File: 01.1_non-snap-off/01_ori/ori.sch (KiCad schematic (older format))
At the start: 141 parts, among them J1 TYPE-C-31-M12_13, J2 AVR-ISP-6_mod, K1 KEYSW, K10 KEYSW, K11 KEYSW, K12 KEYSW, K13 KEYSW, K14 KEYSW, K15 KEYSW, K16 KEYSW, K17 KEYSW, K18 KEYSW, K19 KEYSW, K2 KEYSW, K20 KEYSW, K21 KEYSW, K22 KEYSW, K23 KEYSW, K24 KEYSW, K25 KEYSW, K26 KEYSW, K27 KEYSW, K28 KEYSW, K29 KEYSW, K3 KEYSW, K30 KEYSW, K31 KEYSW, K32 KEYSW, K33 KEYSW, K34 KEYSW, K35 KEYSW, K36 KEYSW, K37 KEYSW, K38 KEYSW, K39 KEYSW, K4 KEYSW, K40 KEYSW, K41 KEYSW, K42 KEYSW, K43 KEYSW, K44 KEYSW, K45 KEYSW, K46 KEYSW, K47 KEYSW, K48 KEYSW, K49 KEYSW, K5 KEYSW, K50 KEYSW, K51 KEYSW, K52 KEYSW, K6 KEYSW, K7 KEYSW, K8 KEYSW, K9 KEYSW, SW1 SW_PUSH, SW2 Rotary_Encoder_Switch, U1 ATMEGA32U4, U3 USBLC6-2SC6, Y1 16MHz

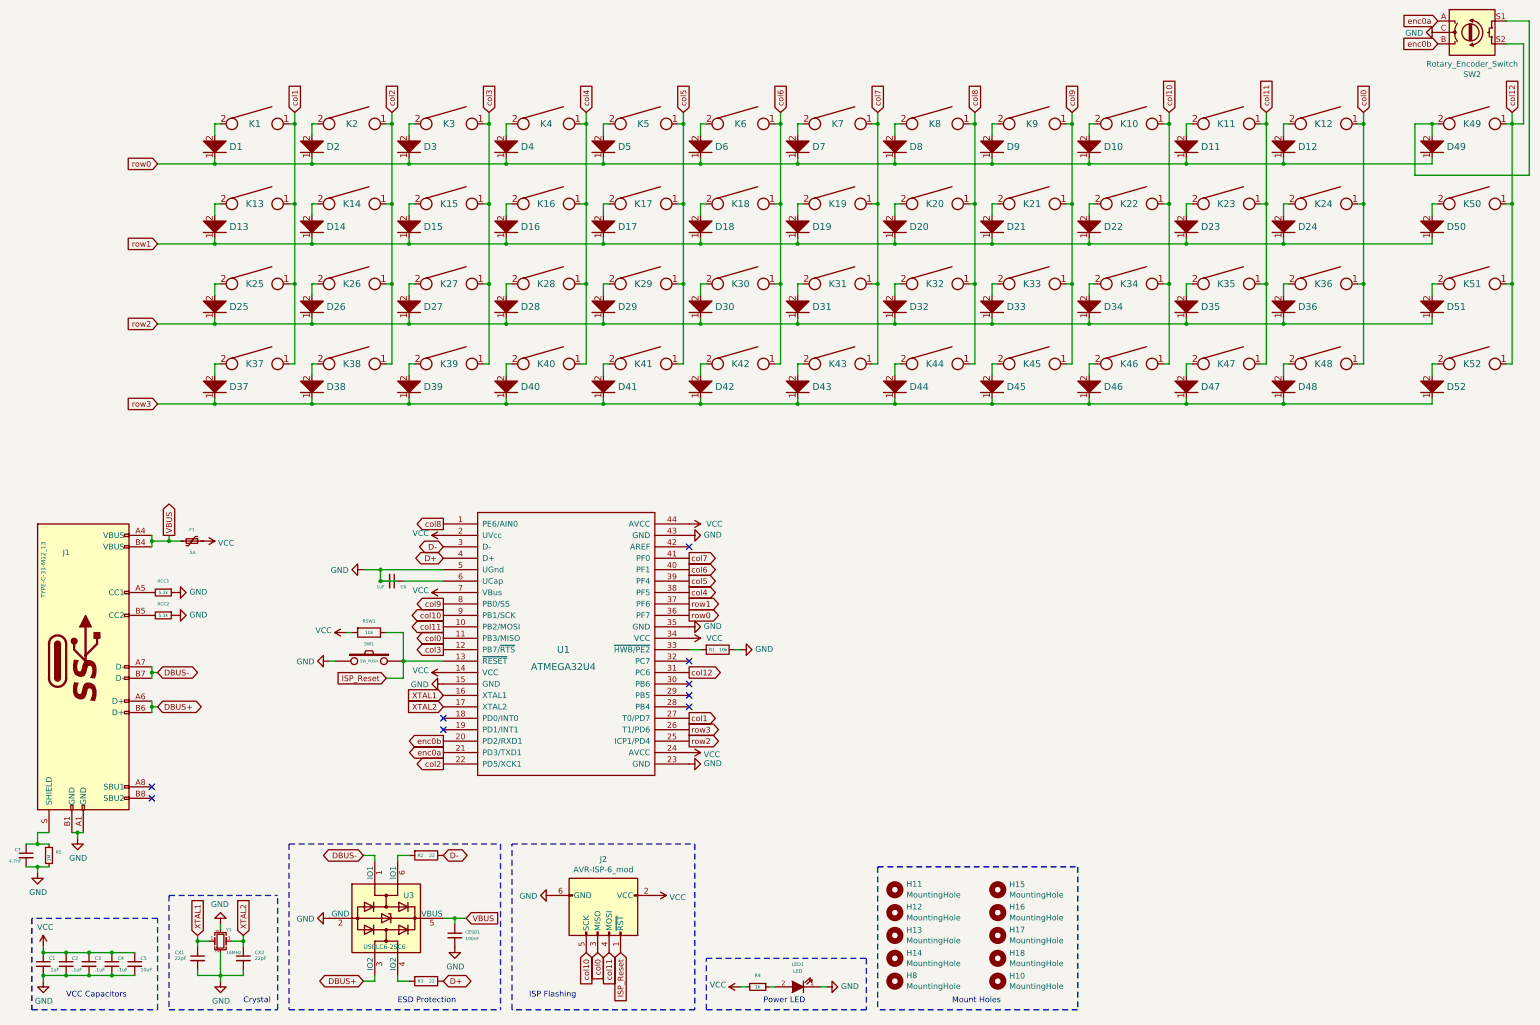
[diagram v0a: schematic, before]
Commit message: update column names
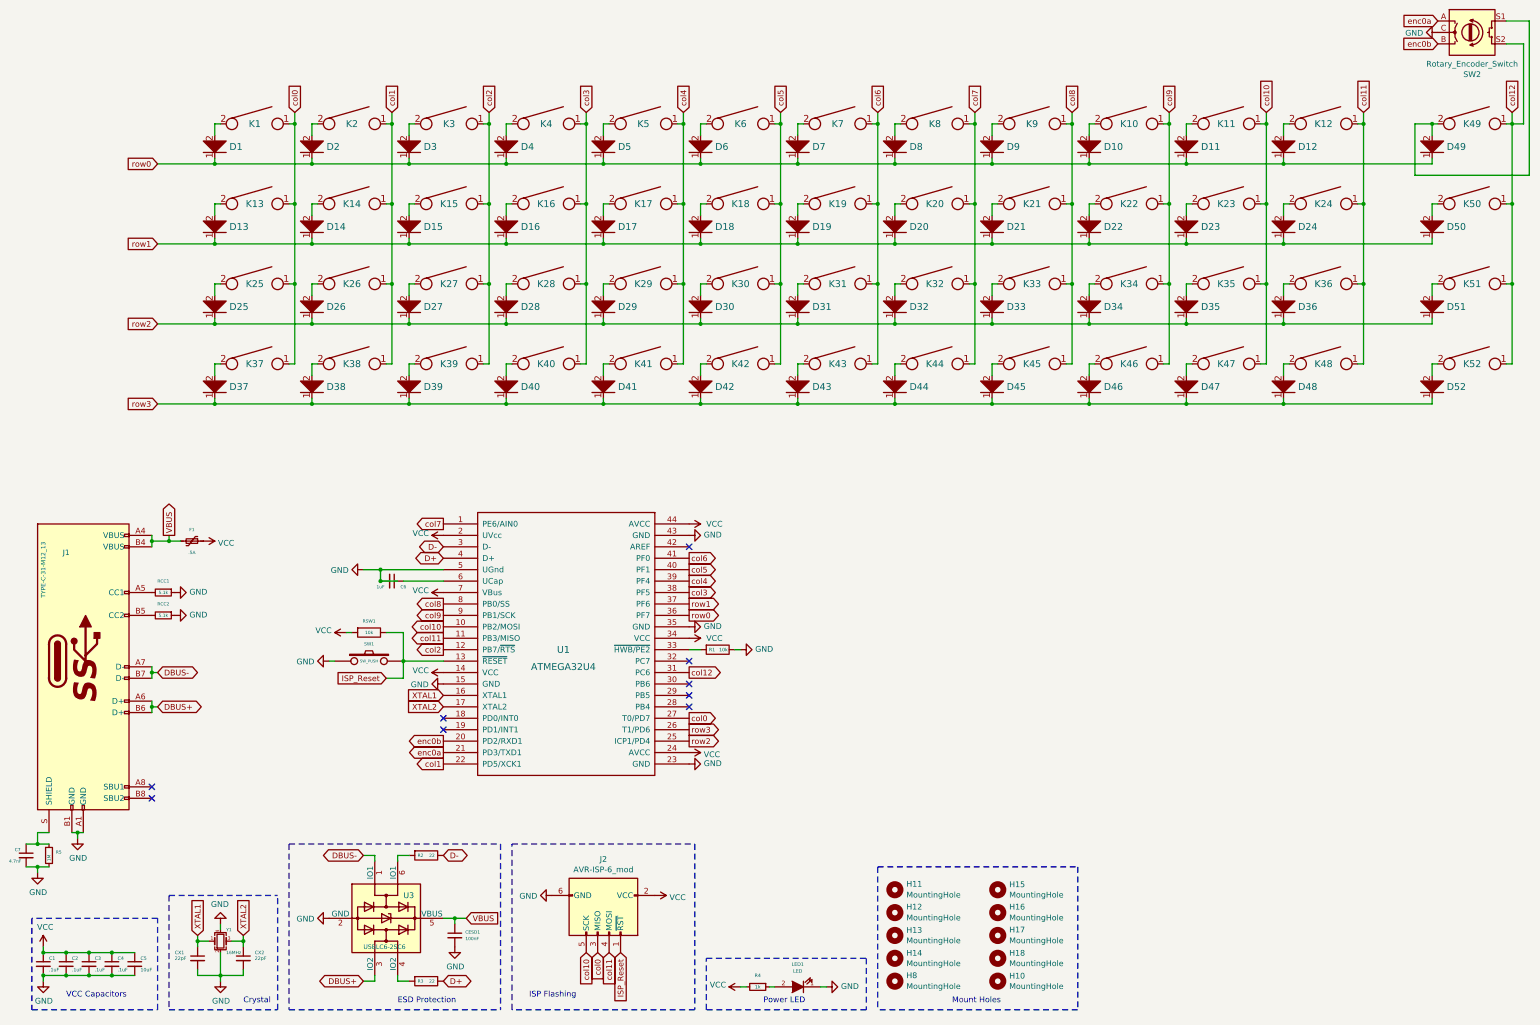
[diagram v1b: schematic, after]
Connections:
- net col0: now also K1.1, K13.1, K25.1, K37.1, U1.27 (T0/PD7); no longer K12.1, K24.1, K36.1, K48.1, U1.11 (PB3/MISO)
- net col1: now also K14.1, K2.1, K26.1, K38.1, U1.22 (PD5/XCK1); no longer K1.1, K13.1, K25.1, K37.1, U1.27 (T0/PD7)
- net col10: now also K11.1, K23.1, K35.1, K47.1, U1.10 (PB2/MOSI); no longer K10.1, K22.1, K34.1, K46.1, U1.9 (PB1/SCK)
- net col11: now also K12.1, K24.1, K36.1, K48.1, U1.11 (PB3/MISO); no longer K11.1, K23.1, K35.1, K47.1, U1.10 (PB2/MOSI)
- net col2: now also K15.1, K27.1, K3.1, K39.1, U1.12 (PB7/~RTS); no longer K14.1, K2.1, K26.1, K38.1, U1.22 (PD5/XCK1)
- net col3: now also K16.1, K28.1, K4.1, K40.1, U1.38 (PF5); no longer K15.1, K27.1, K3.1, K39.1, U1.12 (PB7/~RTS)
- net col4: now also K17.1, K29.1, K41.1, K5.1, U1.39 (PF4); no longer K16.1, K28.1, K4.1, K40.1, U1.38 (PF5)
- net col5: now also K18.1, K30.1, K42.1, K6.1, U1.40 (PF1); no longer K17.1, K29.1, K41.1, K5.1, U1.39 (PF4)
- net col6: now also K19.1, K31.1, K43.1, K7.1, U1.41 (PF0); no longer K18.1, K30.1, K42.1, K6.1, U1.40 (PF1)
- net col7: now also K20.1, K32.1, K44.1, K8.1, U1.1 (PE6/AIN0); no longer K19.1, K31.1, K43.1, K7.1, U1.41 (PF0)
- net col8: now also K21.1, K33.1, K45.1, K9.1, U1.8 (PB0/SS); no longer K20.1, K32.1, K44.1, K8.1, U1.1 (PE6/AIN0)
- net col9: now also K10.1, K22.1, K34.1, K46.1, U1.9 (PB1/SCK); no longer K21.1, K33.1, K45.1, K9.1, U1.8 (PB0/SS)
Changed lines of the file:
@@
 row1
 Text GLabel 5300 7400 0    50   Output ~ 0
+col1
+Text GLabel 5300 6400 0    50   Output ~ 0
 col2
-Text GLabel 5300 6400 0    50   Output ~ 0
-col3
 Text GLabel 5300 6200 0    50   Output ~ 0
-col11
+col10
 Text GLabel 5300 6100 0    50   Output ~ 0
-col10
+col9
 Text GLabel 5300 6000 0    50   Output ~ 0
-col9
+col8
 Text GLabel 5300 5300 0    50   Output ~ 0
-col8
+col7
 Text GLabel 7450 6100 2    50   Output ~ 0
 row0
@@
 $EndComp
 Text GLabel 7450 5800 2    50   Output ~ 0
+col4
+Text GLabel 7450 5700 2    50   Output ~ 0
 col5
-Text GLabel 7450 5700 2    50   Output ~ 0
-col6
-Text GLabel 7450 5600 2    50   Output ~ 0
-col7
 NoConn ~ 7450 5500
 Text GLabel 5300 9300 2    50   BiDi ~ 0
@@
 $EndComp
 Text GLabel 7450 5900 2    50   Output ~ 0
-col4
+col3
 Text GLabel 7450 7100 2    50   Output ~ 0
 row3
@@
 $EndComp
 Connection ~ 14650 2500
-Text GLabel 13350 1700 1    50   Input ~ 0
-col0
-Text GLabel 5300 6300 0    50   Output ~ 0
+Text GLabel 4000 1700 1    50   Input ~ 0
 col0
 Wire Wire Line
@@
 	13350 2500 13350 3200
 Connection ~ 13350 2500
-Text GLabel 4000 1700 1    50   Input ~ 0
+Text GLabel 4850 1700 1    50   Input ~ 0
 col1
-Text GLabel 4850 1700 1    50   Input ~ 0
+Text GLabel 5700 1700 1    50   Input ~ 0
 col2
-Text GLabel 5700 1700 1    50   Input ~ 0
+Text GLabel 6550 1700 1    50   Input ~ 0
 col3
-Text GLabel 6550 1700 1    50   Input ~ 0
+Text GLabel 7400 1700 1    50   Input ~ 0
 col4
-Text GLabel 7400 1700 1    50   Input ~ 0
+Text GLabel 8250 1700 1    50   Input ~ 0
 col5
-Text GLabel 8250 1700 1    50   Input ~ 0
+Text GLabel 9100 1700 1    50   Input ~ 0
 col6
-Text GLabel 9100 1700 1    50   Input ~ 0
+Text GLabel 9950 1700 1    50   Input ~ 0
 col7
-Text GLabel 9950 1700 1    50   Input ~ 0
+Text GLabel 10800 1700 1    50   Input ~ 0
 col8
-Text GLabel 10800 1700 1    50   Input ~ 0
+Text GLabel 11650 1700 1    50   Input ~ 0
 col9
-Text GLabel 11650 1700 1    50   Input ~ 0
-col10
-Text GLabel 12500 1700 1    50   Input ~ 0
+Text GLabel 13350 1700 1    50   Input ~ 0
 col11
 Text GLabel 14650 1700 1    50   Input ~ 0
@@
 enc0a
 Text GLabel 7450 7000 2    50   Output ~ 0
-col1
+col0
 Text GLabel 2800 4250 0    50   Input ~ 0
 row3
@@
 Wire Notes Line
 	9100 8300 9100 9550
+Text GLabel 12500 1700 1    50   Input ~ 0
+col10
+Text GLabel 5300 6300 0    50   Output ~ 0
+col11
+Text GLabel 7450 5600 2    50   Output ~ 0
+col6
 $EndSCHEMATC

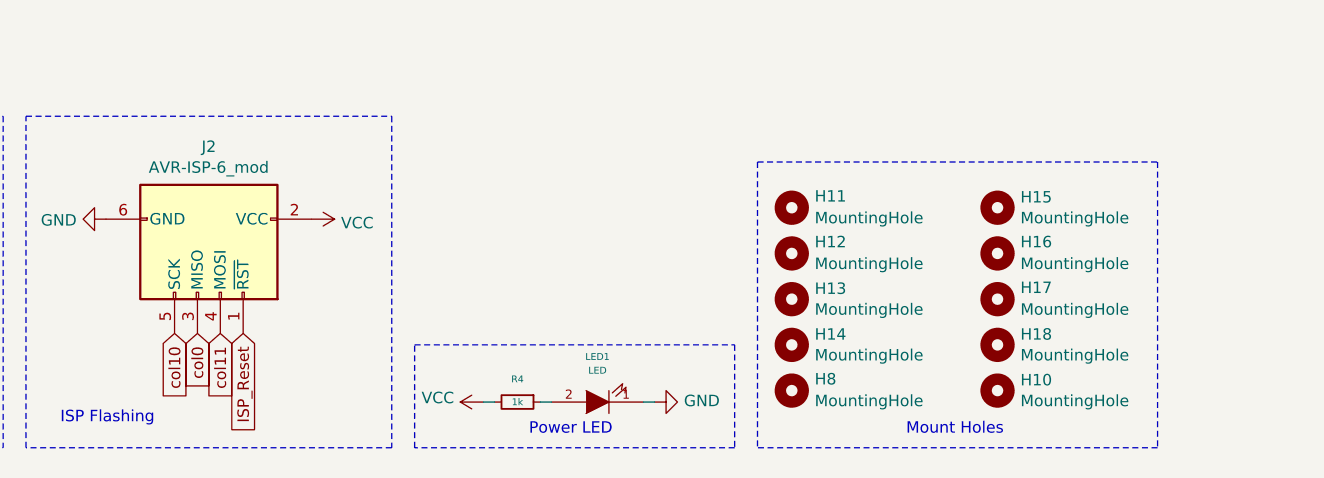
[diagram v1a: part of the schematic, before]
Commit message: moved mounting holes
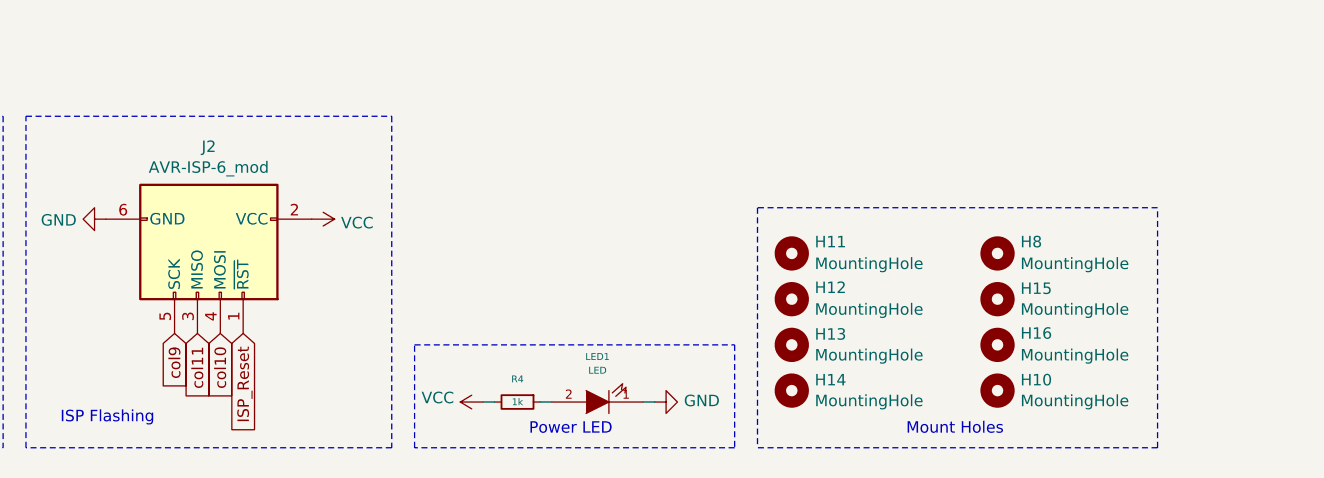
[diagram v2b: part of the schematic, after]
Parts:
- removed H17, H18: MountingHole, random-keyboard-parts:plate_hole_4mm_tht, symbol Mechanical:MountingHole
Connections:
- net col0: no longer J2.3 (MISO)
- net col10: now also J2.4 (MOSI); no longer J2.5 (SCK)
- net col11: now also J2.3 (MISO); no longer J2.4 (MOSI)
- net col9: now also J2.5 (SCK)
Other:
- moved on the sheet: H11, H12, H13, H14, H15, H16, H8
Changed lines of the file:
@@
 L Mechanical:MountingHole H8
 U 1 1 5F26174E
-P 9250 9300
-F 0 "H8" H 9350 9350 50  0000 L CNN
-F 1 "MountingHole" H 9350 9255 50  0000 L CNN
-F 2 "random-keyboard-parts:plate_hole_4mm_tht" H 9250 9300 50  0001 C CNN
-F 3 "~" H 9250 9300 50  0001 C CNN
-	1    9250 9300
+P 10150 8700
+F 0 "H8" H 10250 8750 50  0000 L CNN
+F 1 "MountingHole" H 10250 8655 50  0000 L CNN
+F 2 "random-keyboard-parts:plate_hole_4mm_tht" H 10150 8700 50  0001 C CNN
+F 3 "~" H 10150 8700 50  0001 C CNN
+	1    10150 8700
 	1    0    0    -1
 $EndComp
@@
 	1    0    0    -1
 $EndComp
-Wire Notes Line
-	9100 8300 10850 8300
 Text Notes 9750 9500 0    50   ~ 0
 Mount Holes
 $Comp
-L Mechanical:MountingHole H17
-U 1 1 5EC1BF9B
+L Mechanical:MountingHole H15
+U 1 1 5EC1BF95
 P 10150 8900
-F 0 "H17" H 10250 8950 50  0000 L CNN
+F 0 "H15" H 10250 8946 50  0000 L CNN
 F 1 "MountingHole" H 10250 8855 50  0000 L CNN
 F 2 "random-keyboard-parts:plate_hole_4mm_tht" H 10150 8900 50  0001 C CNN
@@
 $EndComp
 $Comp
-L Mechanical:MountingHole H15
-U 1 1 5EC1BF95
-P 10150 8500
-F 0 "H15" H 10250 8546 50  0000 L CNN
-F 1 "MountingHole" H 10250 8455 50  0000 L CNN
-F 2 "random-keyboard-parts:plate_hole_4mm_tht" H 10150 8500 50  0001 C CNN
-F 3 "~" H 10150 8500 50  0001 C CNN
-	1    10150 8500
-	1    0    0    -1
-$EndComp
-$Comp
-L Mechanical:MountingHole H18
-U 1 1 5EC1BF8F
+L Mechanical:MountingHole H16
+U 1 1 5EC1BF89
 P 10150 9100
-F 0 "H18" H 10250 9146 50  0000 L CNN
+F 0 "H16" H 10250 9150 50  0000 L CNN
 F 1 "MountingHole" H 10250 9055 50  0000 L CNN
 F 2 "random-keyboard-parts:plate_hole_4mm_tht" H 10150 9100 50  0001 C CNN
@@
 $EndComp
 $Comp
-L Mechanical:MountingHole H16
-U 1 1 5EC1BF89
-P 10150 8700
-F 0 "H16" H 10250 8750 50  0000 L CNN
-F 1 "MountingHole" H 10250 8655 50  0000 L CNN
-F 2 "random-keyboard-parts:plate_hole_4mm_tht" H 10150 8700 50  0001 C CNN
-F 3 "~" H 10150 8700 50  0001 C CNN
-	1    10150 8700
-	1    0    0    -1
-$EndComp
-$Comp
 L Mechanical:MountingHole H12
 U 1 1 5EC1BF83
+P 9250 8900
+F 0 "H12" H 9350 8950 50  0000 L CNN
+F 1 "MountingHole" H 9350 8855 50  0000 L CNN
+F 2 "random-keyboard-parts:plate_hole_4mm_tht" H 9250 8900 50  0001 C CNN
+F 3 "~" H 9250 8900 50  0001 C CNN
+	1    9250 8900
+	1    0    0    -1
+$EndComp
+$Comp
+L Mechanical:MountingHole H14
+U 1 1 5EC1BF7D
+P 9250 9300
+F 0 "H14" H 9350 9346 50  0000 L CNN
+F 1 "MountingHole" H 9350 9255 50  0000 L CNN
+F 2 "random-keyboard-parts:plate_hole_4mm_tht" H 9250 9300 50  0001 C CNN
+F 3 "~" H 9250 9300 50  0001 C CNN
+	1    9250 9300
+	1    0    0    -1
+$EndComp
+$Comp
+L Mechanical:MountingHole H13
+U 1 1 5EC1BF77
+P 9250 9100
+F 0 "H13" H 9350 9146 50  0000 L CNN
+F 1 "MountingHole" H 9350 9055 50  0000 L CNN
+F 2 "random-keyboard-parts:plate_hole_4mm_tht" H 9250 9100 50  0001 C CNN
+F 3 "~" H 9250 9100 50  0001 C CNN
+	1    9250 9100
+	1    0    0    -1
+$EndComp
+$Comp
+L Mechanical:MountingHole H11
+U 1 1 5EC1BF71
 P 9250 8700
-F 0 "H12" H 9350 8750 50  0000 L CNN
+F 0 "H11" H 9350 8750 50  0000 L CNN
 F 1 "MountingHole" H 9350 8655 50  0000 L CNN
 F 2 "random-keyboard-parts:plate_hole_4mm_tht" H 9250 8700 50  0001 C CNN
 F 3 "~" H 9250 8700 50  0001 C CNN
 	1    9250 8700
-	1    0    0    -1
-$EndComp
-$Comp
-L Mechanical:MountingHole H14
-U 1 1 5EC1BF7D
-P 9250 9100
-F 0 "H14" H 9350 9146 50  0000 L CNN
-F 1 "MountingHole" H 9350 9055 50  0000 L CNN
-F 2 "random-keyboard-parts:plate_hole_4mm_tht" H 9250 9100 50  0001 C CNN
-F 3 "~" H 9250 9100 50  0001 C CNN
-	1    9250 9100
-	1    0    0    -1
-$EndComp
-$Comp
-L Mechanical:MountingHole H13
-U 1 1 5EC1BF77
-P 9250 8900
-F 0 "H13" H 9350 8946 50  0000 L CNN
-F 1 "MountingHole" H 9350 8855 50  0000 L CNN
-F 2 "random-keyboard-parts:plate_hole_4mm_tht" H 9250 8900 50  0001 C CNN
-F 3 "~" H 9250 8900 50  0001 C CNN
-	1    9250 8900
-	1    0    0    -1
-$EndComp
-$Comp
-L Mechanical:MountingHole H11
-U 1 1 5EC1BF71
-P 9250 8500
-F 0 "H11" H 9350 8550 50  0000 L CNN
-F 1 "MountingHole" H 9350 8455 50  0000 L CNN
-F 2 "random-keyboard-parts:plate_hole_4mm_tht" H 9250 8500 50  0001 C CNN
-F 3 "~" H 9250 8500 50  0001 C CNN
-	1    9250 8500
 	1    0    0    -1
 $EndComp
@@
 $EndComp
 Text GLabel 6650 9050 3    50   Input ~ 0
-col0
+col11
 Text GLabel 6750 9050 3    50   Input ~ 0
-col11
+col10
 $Comp
 L power:GND #PWR0101
@@
 D-
 Text GLabel 6550 9050 3    50   Input ~ 0
-col10
+col9
 Text GLabel 6850 9050 3    50   Input ~ 0
 ISP_Reset
@@
 Wire Notes Line
 	10850 9550 9100 9550
-Wire Notes Line
-	10850 8300 10850 9550
-Wire Notes Line
-	9100 8300 9100 9550
 Text GLabel 12500 1700 1    50   Input ~ 0
 col10
@@
 Text GLabel 7450 5600 2    50   Output ~ 0
 col6
+Wire Notes Line
+	10850 9550 10850 8500
+Wire Notes Line
+	10850 8500 9100 8500
+Wire Notes Line
+	9100 8500 9100 9550
 $EndSCHEMATC
